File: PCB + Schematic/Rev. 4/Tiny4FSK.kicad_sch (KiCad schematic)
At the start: 67 parts, among them IC1 SI4063, J1 SWD, J2 GPIO, J4 USB, J5 I2C, J6 Power, J7 SPI, SW1 RST, SW2 BATT PWR, U1 ATSAMD21G18A-A, U2 ATGM336H, U2 TPS61200DRC, U5 1XZA032768AD19

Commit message: Inductors
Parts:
- L1, L4: LCSC (none) -> C307609
- L3: footprint Inductor_SMD:L_0603_1608Metric_Pad1.05x0.95mm_HandSolder -> Inductor_SMD:L_0402_1005Metric_Pad0.77x0.64mm_HandSolder; LCSC (none) -> C275307
- L5: LCSC C330865 -> C341687
- L6: LCSC C408700 -> C167476
- L7: LCSC (none) -> C86129
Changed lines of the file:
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@@
 			)
 		)
+		(property "LCSC" "C307609"
+			(at 40.64 38.1 90)
+			(effects
+				(font
+					(size 1.27 1.27)
+				)
+				(hide yes)
+			)
+		)
 		(pin "1"
 		)
@@
 			)
 		)
+		(property "LCSC" "C86129"
+			(at 63.5 38.1 90)
+			(effects
+				(font
+					(size 1.27 1.27)
+				)
+				(hide yes)
+			)
+		)
 		(pin "1"
 		)
@@
 			)
 		)
-		(property "LCSC" "C408700"
+		(property "LCSC" "C167476"
 			(at 55.88 38.1 90)
 			(effects
@@
 			)
 		)
-		(property "Footprint" "Inductor_SMD:L_0603_1608Metric_Pad1.05x0.95mm_HandSolder"
+		(property "Footprint" "Inductor_SMD:L_0402_1005Metric_Pad0.77x0.64mm_HandSolder"
 			(at 25.4 34.29 0)
 			(effects
@@
 			)
 		)
+		(property "LCSC" "C275307"
+			(at 25.4 34.29 0)
+			(effects
+				(font
+					(size 1.27 1.27)
+				)
+				(hide yes)
+			)
+		)
 		(pin "1"
 		)
@@
 			)
 		)
-		(property "LCSC" "C330865"
+		(property "LCSC" "C341687"
 			(at 48.26 38.1 90)
 			(effects
@@
 			(effects
 				(font
+					(size 1.27 1.27)
+				)
+				(hide yes)
+			)
+		)
+		(property "LCSC" "C307609"
+			(at 68.58 71.12 90)
+			(effects
+				(font

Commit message: Update PCB, add more jlcpcb parts
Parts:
- R10, R13, R9: LCSC (none) -> C23138
- SW1: LCSC (none) -> C2888954
- SW2: LCSC (none) -> C963206
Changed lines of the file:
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@@
 			)
 		)
+		(property "LCSC" "C23138"
+			(at 114.3 139.7 0)
+			(effects
+				(font
+					(size 1.27 1.27)
+				)
+				(hide yes)
+			)
+		)
 		(pin "1"
 		)
@@
 			)
 		)
+		(property "LCSC" "C23138"
+			(at 144.78 113.03 90)
+			(effects
+				(font
+					(size 1.27 1.27)
+				)
+				(hide yes)
+			)
+		)
 		(pin "1"
 		)
@@
 			)
 		)
+		(property "LCSC" "C2888954"
+			(at 180.34 179.07 0)
+			(effects
+				(font
+					(size 1.27 1.27)
+				)
+				(hide yes)
+			)
+		)
 		(pin "1"
 		)
@@
 			)
 		)
+		(property "LCSC" "C23138"
+			(at 134.62 113.03 90)
+			(effects
+				(font
+					(size 1.27 1.27)
+				)
+				(hide yes)
+			)
+		)
 		(pin "1"
 		)
@@
 			(at 144.526 138.43 0)
 			(effects
+				(font
+					(size 1.27 1.27)
+				)
+				(hide yes)
+			)
+		)
+		(property "LCSC" "C963206"
+			(at 144.526 138.43 0)
+			(effects

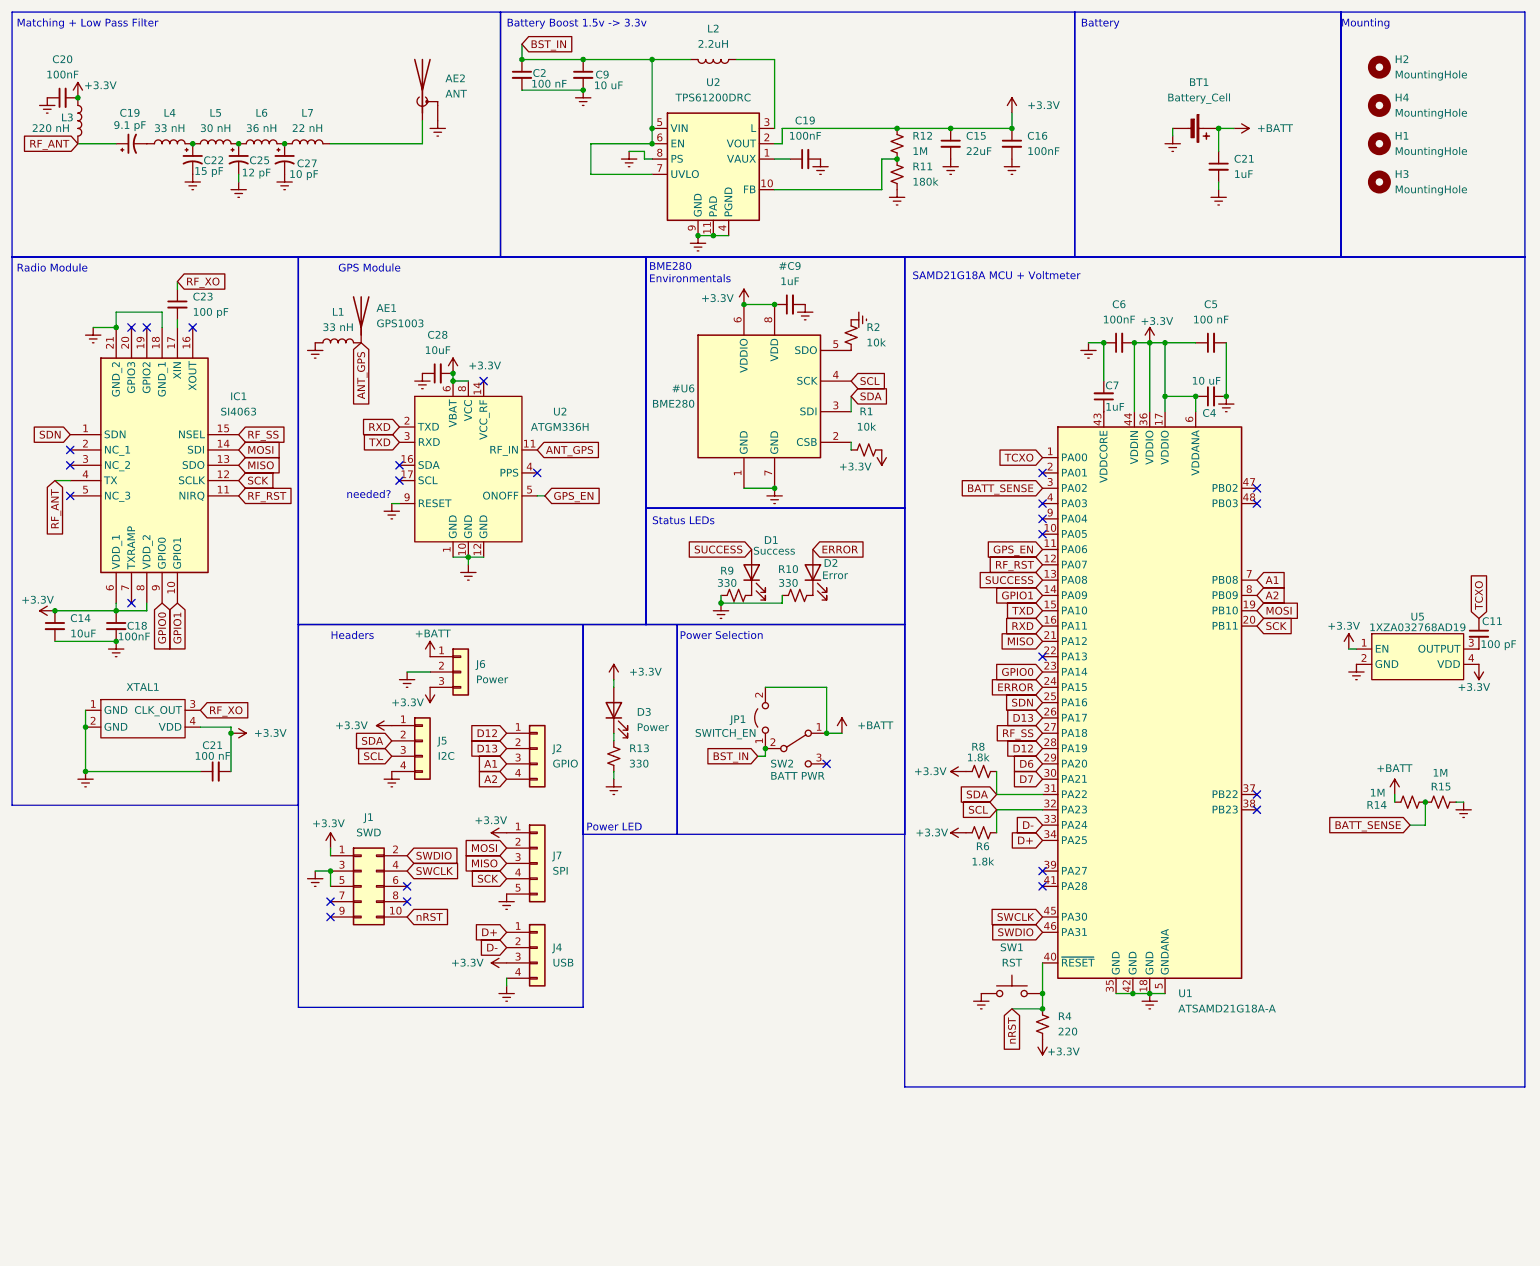
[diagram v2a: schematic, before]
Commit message: Neaten up schematic, add breakaway tabs and stitching vias
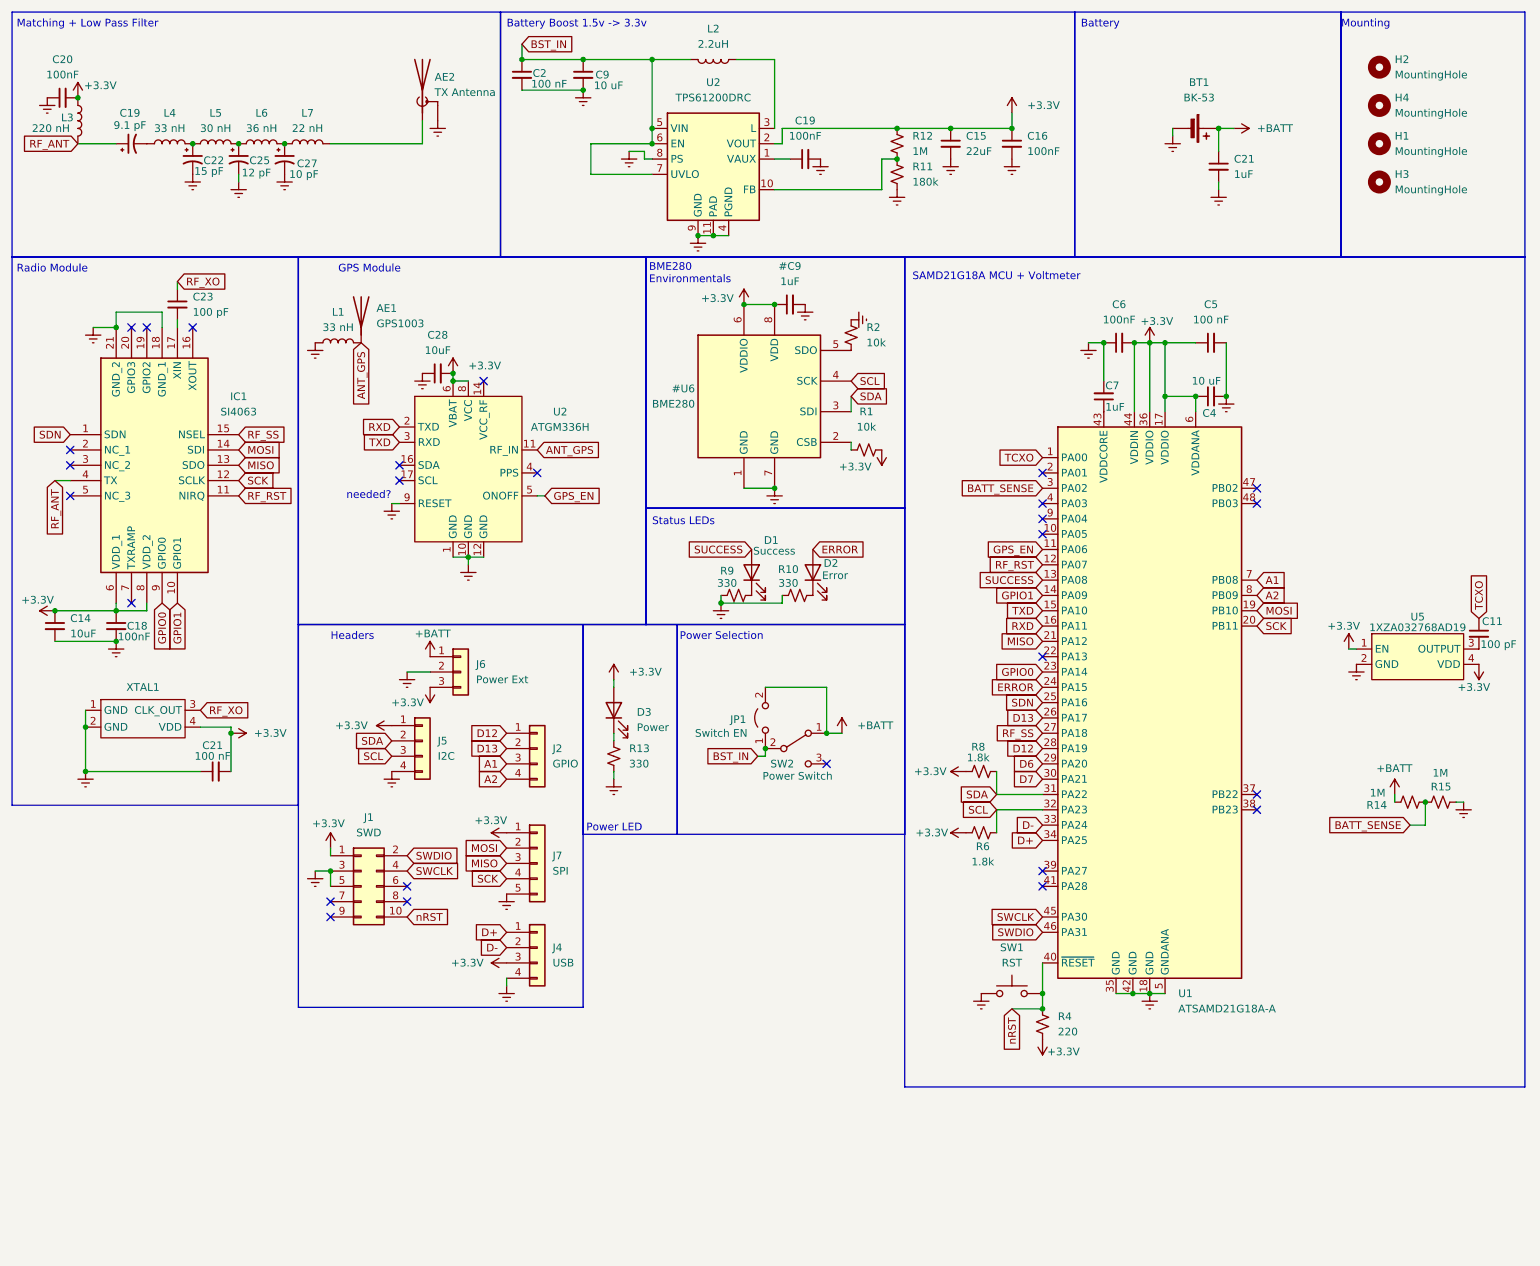
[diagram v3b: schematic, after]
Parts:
- AE2: value ANT -> TX Antenna
- BT1: value Battery_Cell -> BK-53
- J6: value Power -> Power Ext
- JP1: value SWITCH_EN -> Switch EN
- R14: LCSC C26083 -> C26083
- SW2: value BATT PWR -> Power Switch
- XTAL1: LCSC (none) -> C135223
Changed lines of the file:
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@@
 			)
 		)
-		(property "Value" "SWITCH_EN"
+		(property "Value" "Switch EN"
 			(at 127.762 135.89 90)
 			(effects
@@
 			)
 		)
-		(property "Value" "Power"
+		(property "Value" "Power Ext"
 			(at 91.44 126.9999 0)
 			(effects
@@
 			)
 		)
-		(property "LCSC" "C26083 "
+		(property "LCSC" "C26083"
 			(at 246.38 147.32 90)
 			(effects
@@
 			)
 		)
+		(property "LCSC" "C135223"
+			(at 38.354 130.048 0)
+			(effects
+				(font
+					(size 1.27 1.27)
+				)
+				(hide yes)
+			)
+		)
 		(pin "1"
 		)
@@
 		(on_board yes)
 		(dnp no)
-		(fields_autoplaced yes)
 		(property "Reference" "AE2"
-			(at 86.36 27.3049 0)
+			(at 84.582 27.0509 0)
 			(effects
 				(font
@@
 			)
 		)
-		(property "Value" "ANT"
-			(at 86.36 29.8449 0)
+		(property "Value" "TX Antenna"
+			(at 84.582 29.5909 0)
 			(effects
 				(font
@@
 			)
 		)
-		(property "Value" "Battery_Cell"
+		(property "Value" "BK-53"
 			(at 211.3915 30.48 90)
 			(effects
@@
 			)
 		)
-		(property "Value" "BATT PWR"
+		(property "Value" "Power Switch"
 			(at 144.78 143.002 0)
 			(effects

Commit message: Reference designators
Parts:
- renumbered IC1 to U3, XTAL1 to U7
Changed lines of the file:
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@@
 		(dnp no)
 		(fields_autoplaced yes)
-		(property "Reference" "IC1"
+		(property "Reference" "U3"
 			(at 52.07 80.0414 0)
 			(effects
@@
 			(project "Tiny4FSK"
 				(path "/afd8b0bc-328a-481f-8ddf-c1252dc3b440"
-					(reference "IC1")
+					(reference "U3")
 					(unit 1)
 				)
@@
 		(dnp no)
 		(fields_autoplaced yes)
-		(property "Reference" "XTAL1"
+		(property "Reference" "U7"
 			(at 36.195 128.27 0)
 			(effects
@@
 			(project "Tiny4FSK"
 				(path "/afd8b0bc-328a-481f-8ddf-c1252dc3b440"
-					(reference "XTAL1")
-					(unit 1)
-				)
+					(reference "U7")
+					(unit 1)
+				)

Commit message: USB, 3D models, Reference Designators
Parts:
- added C1: 4.5 nF, Capacitor_SMD:C_0805_2012Metric_Pad1.18x1.45mm_HandSolder, symbol Device:C_Small
- added C3, C4: 100 nF, Capacitor_SMD:C_0805_2012Metric_Pad1.18x1.45mm_HandSolder, symbol Device:C_Small
- added C5, C6: 1uF, Capacitor_SMD:C_0805_2012Metric_Pad1.18x1.45mm_HandSolder, symbol Device:C_Small
- added FB1: BLM18AG121SN1D, Resistor_SMD:R_0603_1608Metric_Pad0.98x0.95mm_HandSolder, symbol Device:FerriteBead_Small
- added J3: USBC, Connector_USB:USB_C_Receptacle_GCT_USB4105-xx-A_16P_TopMnt_Horizontal, symbol Connector:USB_C_Receptacle_USB2.0
- added J8: USB, Connector_PinHeader_2.54mm:PinHeader_1x04_P2.54mm_Vertical, symbol Connector_Generic:Conn_01x04
- added R3: 1M, Resistor_SMD:R_0805_2012Metric_Pad1.20x1.40mm_HandSolder, symbol Device:R_Small_US
- added R5, R7: 5k1, Resistor_SMD:R_0805_2012Metric_Pad1.20x1.40mm_HandSolder, symbol Device:R_Small_US
- added U8: Linear Step-Down, LDO:MCP1700, symbol Regulator_Linear:MCP1700x-330xxTT
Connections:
- net D+: now also J3.A6 (D+), J3.B6 (D+), J8.1 (Pin_1)
- net D-: now also J3.A7 (D-), J3.B7 (D-), J8.2 (Pin_2)
- net Earth: now also C1.1, C3.2, C4.2, C5.1, C6.2, J3.A1 (GND), J3.A12 (GND), J3.B1 (GND), J3.B12 (GND), J8.4 (Pin_4), R3.2, R5.1, R7.1, U8.1 (GND)
- new net: J3.B5 (CC2), R7.2
- new net: J3.A5 (CC1), R5.2
- new net: C1.2, J3.S1 (SHIELD), R3.1
- new net LDO: C6.1, J8.3 (Pin_3), U8.2 (VO)
- new net LIN: C4.1, C5.2, FB1.2, U8.3 (VI)
- new net USB: C3.1, FB1.1, J3.A4 (VBUS), J3.A9 (VBUS), J3.B4 (VBUS), J3.B9 (VBUS)
- no-connect marks 27 -> 29

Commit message: FAB output, USB
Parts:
- C1: LCSC (none) -> C1744
- C3, C4: footprint Capacitor_SMD:C_0805_2012Metric_Pad1.18x1.45mm_HandSolder -> Capacitor_SMD:C_0402_1005Metric_Pad0.74x0.62mm_HandSolder; LCSC (none) -> C1525
- C5, C6: footprint Capacitor_SMD:C_0805_2012Metric_Pad1.18x1.45mm_HandSolder -> Capacitor_SMD:C_0402_1005Metric_Pad0.74x0.62mm_HandSolder; LCSC (none) -> C52923
- D3: LCSC (none) -> C84256
- FB1: LCSC (none) -> C76892
- J1, J2, J4, J5, J6, J7, U3: now not fitted
- J3: LCSC (none) -> C136423
- J8: value USB -> USB Breakout
- R3: footprint Resistor_SMD:R_0805_2012Metric_Pad1.20x1.40mm_HandSolder -> Resistor_SMD:R_0402_1005Metric_Pad0.72x0.64mm_HandSolder; LCSC (none) -> C26083
- R5, R7: LCSC (none) -> C27834
- U8: LCSC (none) -> C632000
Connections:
- net LDO is gone; now on net +3.3V: C6.1, J8.3 (Pin_3), U8.2 (VO)
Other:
- moved on the sheet: C5, C6, J8, U8

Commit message: JLCPCB optimization
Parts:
- BT1, J8: now not fitted
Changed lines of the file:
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@@
 		(in_bom yes)
 		(on_board yes)
-		(dnp no)
+		(dnp yes)
 		(property "Reference" "J8"
 			(at 88.9 209.5499 0)
@@
 		(in_bom yes)
 		(on_board yes)
-		(dnp no)
+		(dnp yes)
 		(fields_autoplaced yes)
 		(property "Reference" "BT1"

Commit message: Better Breakaway tabs, JLC export
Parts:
- AE2, JP1: now not fitted
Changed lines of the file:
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@@
 		(in_bom yes)
 		(on_board yes)
-		(dnp no)
+		(dnp yes)
 		(property "Reference" "JP1"
 			(at 133.604 133.604 90)
@@
 		(in_bom yes)
 		(on_board yes)
-		(dnp no)
+		(dnp yes)
 		(property "Reference" "AE2"
 			(at 84.582 27.0509 0)
